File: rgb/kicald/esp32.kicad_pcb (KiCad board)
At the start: 2 copper layers, 90.2 x 49.6 mm, 72 parts, among them J1 5 / 12V, J10 W1, J11 +12V, J12 R2, J13 G2, J14 B2, J15 CONN FT232RL, J16 W2, J17 +12V, J18 R3, J19 G3, J2 +12V, J20 B3, J21 W3, J22 +12V, J23 R4, J24 G4, J25 B4, J26 W1, J3 R1, J4 G1, J5 hole, J6 hole, J7 hole, J8 hole, J9 B1, Q1 ZXMS6004, Q10 ZXMS6004, Q11 ZXMS6004, Q12 ZXMS6004, Q13 ZXMS6004, Q14 ZXMS6004, Q15 ZXMS6004, Q16 ZXMS6004, Q2 ZXMS6004, Q3 ZXMS6004, Q4 ZXMS6004, Q5 ZXMS6004, Q6 ZXMS6004, Q7 ZXMS6004, Q8 ZXMS6004, Q9 ZXMS6004, SW1 RESET, SW2 PROG, U1 ESP32-WROOM-32U, U2 MS5637, U3 Si7020-A20, U4 PCA9685PW, U5 ACT4088, U6 DS18B20, U8 TCS3400

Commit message: chore: update rgb
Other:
- board text added: "B1"
- board text added: "B2"
- board text added: "B3"
- board text added: "B4"
- board text added: "G1"
- board text added: "G2"
- board text added: "G3"
- board text added: "G4"
- board text added: "R1"
- board text added: "R2"
- board text added: "R3"
- board text added: "R4"
- board text added: "W1"
- board text added: "W2"
- board text added: "W3"
- board text added: "W4"
- board text removed: "GND"
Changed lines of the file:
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@@
   (general
     (thickness 1.6)
-    (drawings 20)
+    (drawings 40)
     (tracks 504)
     (zones 0)
@@
     (pad_to_mask_clearance 0)
     (solder_mask_min_width 0.25)
-    (aux_axis_origin 0 0)
+    (aux_axis_origin 78 111.6)
     (grid_origin 163.09 62.07)
     (visible_elements FFFDFF7F)
@@
     (tags SOT-23)
     (attr smd)
-    (fp_text reference Q4 (at 0 -2.5 90) (layer F.SilkS)
+    (fp_text reference Q4 (at 4.572 -0.254 180) (layer F.SilkS)
       (effects (font (size 1 1) (thickness 0.15)))
     )
@@
     (tags SOT-23)
     (attr smd)
-    (fp_text reference Q3 (at 0 -2.5 90) (layer F.SilkS)
+    (fp_text reference Q3 (at 4.572 0 180) (layer F.SilkS)
       (effects (font (size 1 1) (thickness 0.15)))
     )
@@
     (tags SOT-23)
     (attr smd)
-    (fp_text reference Q2 (at 0 -2.5 90) (layer F.SilkS)
+    (fp_text reference Q2 (at 4.572 0 180) (layer F.SilkS)
       (effects (font (size 1 1) (thickness 0.15)))
     )
@@
     (tags SOT-23)
     (attr smd)
-    (fp_text reference Q1 (at 0 -2.5 90) (layer F.SilkS)
+    (fp_text reference Q1 (at 2.286 0 180) (layer F.SilkS)
       (effects (font (size 1 1) (thickness 0.15)))
     )
@@
       (net 2 +3V3))
   )
+  (dimension 49.6 (width 0.15) (layer F.SilkS)
+    (gr_text "49.600 mm" (at 72.128 86.8 90) (layer F.SilkS)
+      (effects (font (size 1 1) (thickness 0.15)))
+    )
+    (feature1 (pts (xy 78 62) (xy 72.841579 62)))
+    (feature2 (pts (xy 78 111.6) (xy 72.841579 111.6)))
+    (crossbar (pts (xy 73.428 111.6) (xy 73.428 62)))
+    (arrow1a (pts (xy 73.428 62) (xy 74.014421 63.126504)))
+    (arrow1b (pts (xy 73.428 62) (xy 72.841579 63.126504)))
+    (arrow2a (pts (xy 73.428 111.6) (xy 74.014421 110.473496)))
+    (arrow2b (pts (xy 73.428 111.6) (xy 72.841579 110.473496)))
+  )
+  (dimension 90.17 (width 0.15) (layer F.SilkS)
+    (gr_text "90.170 mm" (at 123.085 125.092) (layer F.SilkS)
+      (effects (font (size 1 1) (thickness 0.15)))
+    )
+    (feature1 (pts (xy 168.17 111.6) (xy 168.17 124.378421)))
+    (feature2 (pts (xy 78 111.6) (xy 78 124.378421)))
+    (crossbar (pts (xy 78 123.792) (xy 168.17 123.792)))
+    (arrow1a (pts (xy 168.17 123.792) (xy 167.043496 124.378421)))
+    (arrow1b (pts (xy 168.17 123.792) (xy 167.043496 123.205579)))
+    (arrow2a (pts (xy 78 123.792) (xy 79.126504 124.378421)))
+    (arrow2b (pts (xy 78 123.792) (xy 79.126504 123.205579)))
+  )
+  (gr_text W4 (at 159.28 110.33) (layer F.SilkS)
+    (effects (font (size 1.5 1.5) (thickness 0.3)))
+  )
+  (gr_text B4 (at 155.47 110.33) (layer F.SilkS)
+    (effects (font (size 1.5 1.5) (thickness 0.3)))
+  )
+  (gr_text G4 (at 151.66 110.33) (layer F.SilkS)
+    (effects (font (size 1.5 1.5) (thickness 0.3)))
+  )
+  (gr_text R4 (at 147.85 110.33) (layer F.SilkS)
+    (effects (font (size 1.5 1.5) (thickness 0.3)))
+  )
+  (gr_text W3 (at 139.976 110.33) (layer F.SilkS)
+    (effects (font (size 1.5 1.5) (thickness 0.3)))
+  )
+  (gr_text B3 (at 136.42 110.33) (layer F.SilkS)
+    (effects (font (size 1.5 1.5) (thickness 0.3)))
+  )
+  (gr_text G3 (at 132.61 110.33) (layer F.SilkS)
+    (effects (font (size 1.5 1.5) (thickness 0.3)))
+  )
+  (gr_text R3 (at 128.8 110.33) (layer F.SilkS)
+    (effects (font (size 1.5 1.5) (thickness 0.3)))
+  )
+  (gr_text W2 (at 120.926 110.33) (layer F.SilkS)
+    (effects (font (size 1.5 1.5) (thickness 0.3)))
+  )
+  (gr_text B2 (at 117.37 110.33) (layer F.SilkS)
+    (effects (font (size 1.5 1.5) (thickness 0.3)))
+  )
+  (gr_text G2 (at 113.56 110.33) (layer F.SilkS)
+    (effects (font (size 1.5 1.5) (thickness 0.3)))
+  )
+  (gr_text R2 (at 109.75 110.33) (layer F.SilkS)
+    (effects (font (size 1.5 1.5) (thickness 0.3)))
+  )
+  (gr_text W1 (at 101.876 110.33) (layer F.SilkS)
+    (effects (font (size 1.5 1.5) (thickness 0.3)))
+  )
+  (gr_text B1 (at 98.32 110.33) (layer F.SilkS)
+    (effects (font (size 1.5 1.5) (thickness 0.3)))
+  )
+  (gr_text 12V (at 144.04 110.33) (layer F.SilkS)
+    (effects (font (size 1.5 1.5) (thickness 0.3)))
+  )
+  (gr_text 12V (at 124.99 110.33) (layer F.SilkS)
+    (effects (font (size 1.5 1.5) (thickness 0.3)))
+  )
+  (gr_text 12V (at 86.636 110.33) (layer F.SilkS)
+    (effects (font (size 1.5 1.5) (thickness 0.3)))
+  )
+  (gr_text 12V (at 105.94 110.33) (layer F.SilkS)
+    (effects (font (size 1.5 1.5) (thickness 0.3)))
+  )
+  (gr_text G1 (at 94.51 110.33) (layer F.SilkS)
+    (effects (font (size 1.5 1.5) (thickness 0.3)))
+  )
+  (gr_text R1 (at 90.827 110.33) (layer F.SilkS)
+    (effects (font (size 1.5 1.5) (thickness 0.3)))
+  )
   (gr_line (start 124.587 76.708) (end 124.587 80.772) (layer F.SilkS) (width 0.2))
   (gr_line (start 107.845 82.39) (end 107.845 63.594) (layer F.SilkS) (width 0.15))
@@
   (gr_line (start 78 68.42) (end 78 80.485) (layer F.SilkS) (width 0.15))
   (gr_line (start 168.17 62.07) (end 151.66 62.07) (layer Edge.Cuts) (width 0.1))
-  (gr_text GND (at 85.344 65.024 90) (layer F.SilkS)
-    (effects (font (size 1.5 1.5) (thickness 0.3)))
-  )
   (gr_text PROG (at 158.01 92.55) (layer F.SilkS)
     (effects (font (size 1.5 1.5) (thickness 0.3)))
@@
     (effects (font (size 1.5 1.5) (thickness 0.3)))
   )
-  (gr_text 12V (at 83.08 97.63) (layer F.SilkS)
+  (gr_text "ESP-32\nRGB 1.0" (at 81.556 99.154 90) (layer F.SilkS)
     (effects (font (size 1.5 1.5) (thickness 0.3)))
   )
-  (gr_text "ESP-32\nRGB 1.0" (at 87.525 103.98) (layer F.SilkS)
-    (effects (font (size 1.5 1.5) (thickness 0.3)))
-  )

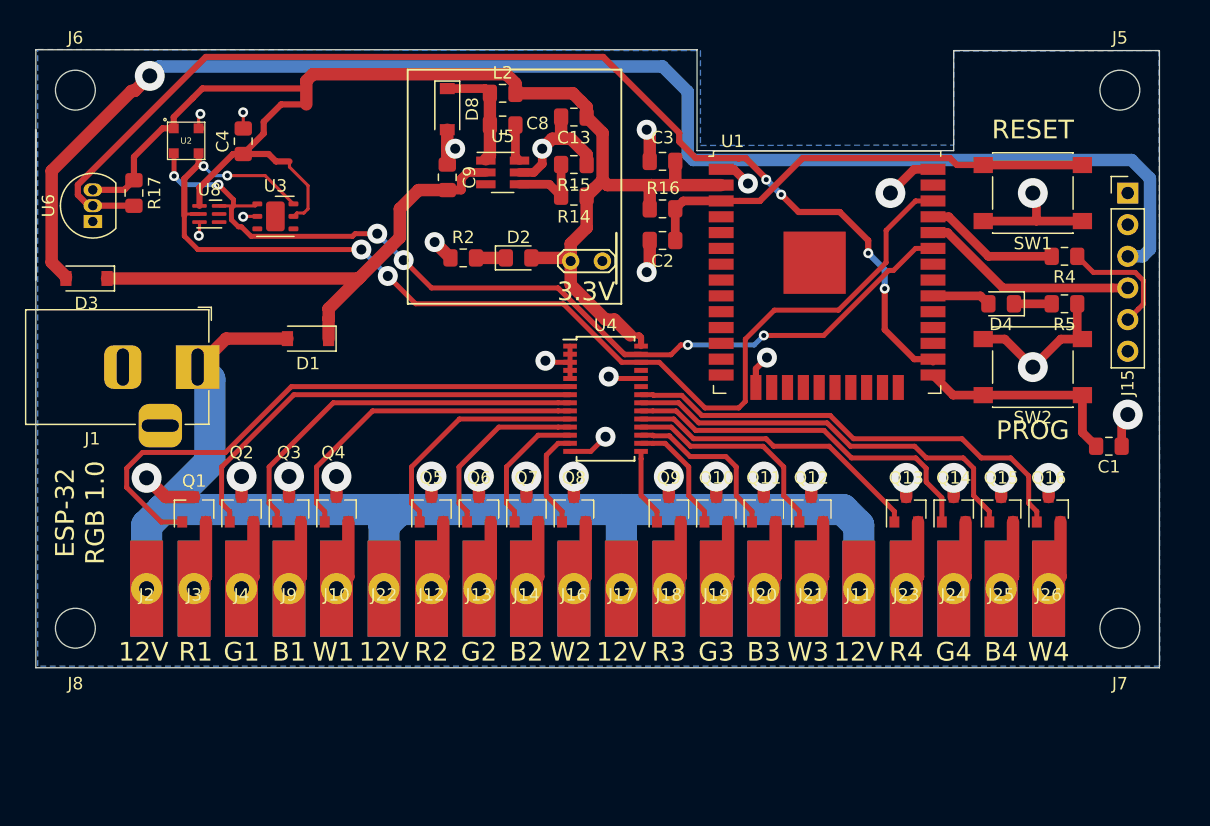
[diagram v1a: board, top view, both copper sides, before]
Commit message: chore: add comment about not usable analogic read
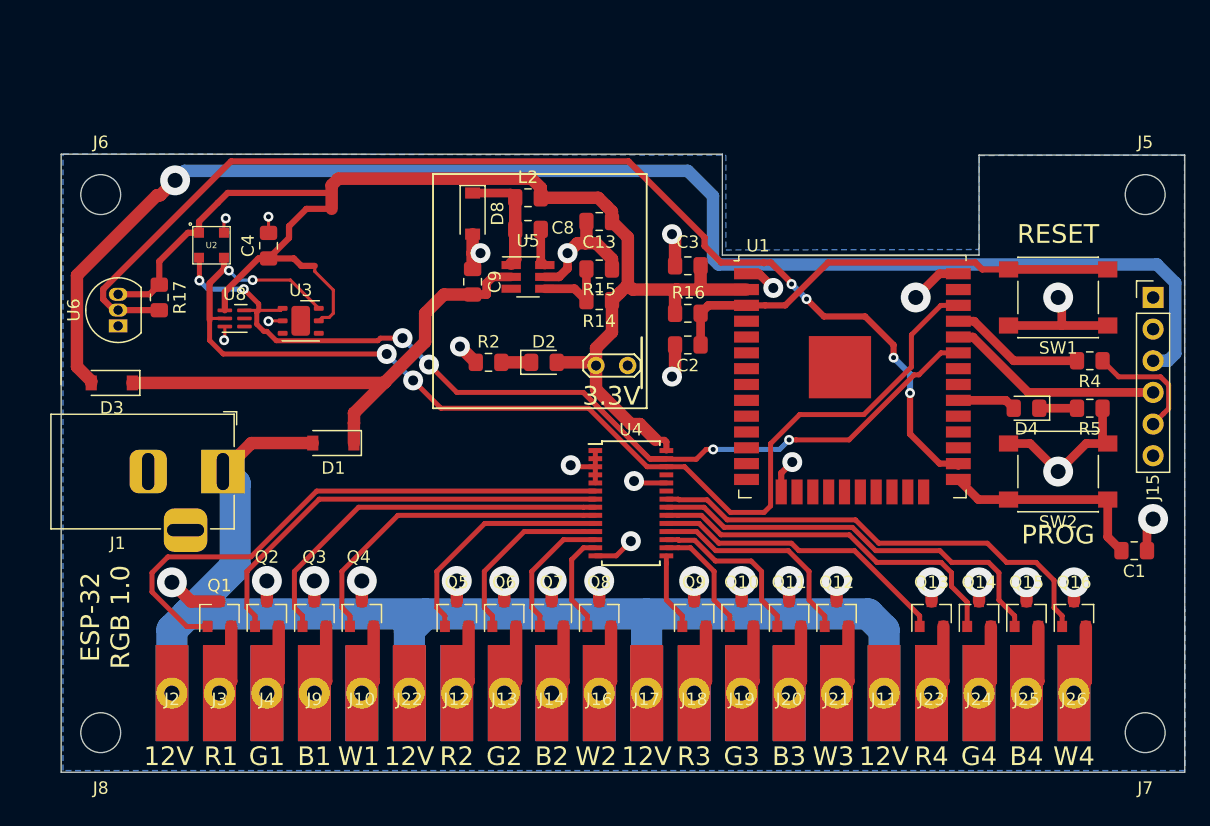
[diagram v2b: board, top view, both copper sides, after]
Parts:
- moved C3 8.62 mm to (130.3, 79.3)
- moved C4 8.62 mm to (96.7, 77.7)
- moved D1 8.62 mm to (101.9, 93.6)
- moved D4 8.62 mm to (157.5, 90.8)
- moved J10 8.62 mm to (104.2, 113.6)
- moved J11 8.62 mm to (146.1, 113.6)
- moved J15 8.62 mm to (167.7, 81.9)
- moved J17 8.62 mm to (127.0, 113.6)
- moved J20 8.62 mm to (138.5, 113.6)
- moved J21 8.62 mm to (142.3, 113.6)
- moved J23 8.62 mm to (149.9, 113.6)
- moved J24 8.62 mm to (153.7, 113.6)
- moved J25 8.62 mm to (157.5, 113.6)
- moved J26 8.62 mm to (161.3, 113.6)
- moved J9 8.62 mm to (100.4, 113.6)
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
